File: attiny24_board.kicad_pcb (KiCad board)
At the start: 2 copper layers, 11 parts, among them J1 SPI, J2 OUT, J3 SCKLED, J4 CONN_01X02, U1 ATTINY24A-SSU, Y1 12000

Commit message: Make changes
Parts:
- moved C1 93.2 mm to (34.3, 32.0)
- moved J4 93.2 mm to (34.3, 20.6)
- moved C2 93.2 mm to (35.8, 26.9)
- moved C3 93.2 mm to (24.6, 27.7)
- moved C4 93.2 mm to (29.0, 27.7)
- moved J1 93.2 mm to (24.1, 45.0)
- moved J3 93.2 mm to (44.5, 20.6)
- moved Y1 93.2 mm to (24.1, 32.0)
- moved D1 93.2 mm to (45.5, 26.7)
- moved J2 93.2 mm to (46.2, 32.3)
- moved U1 93.2 mm to (33.8, 41.6)
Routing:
- net GND: track 62.7 -> 45.5 mm
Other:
- board text added: "+"
- board text added: "-"
- board text added: "LED"
- board text added: "rst"
- board text added: "sck"
- board text added: "si"
- board text added: "so"

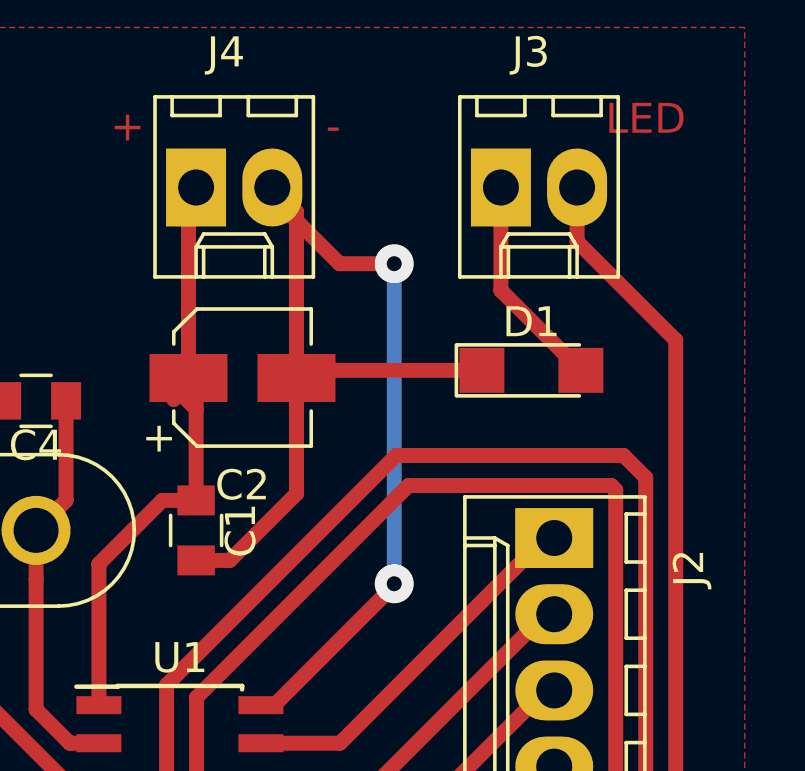
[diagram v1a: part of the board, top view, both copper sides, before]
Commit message: Add forgoteen resistor
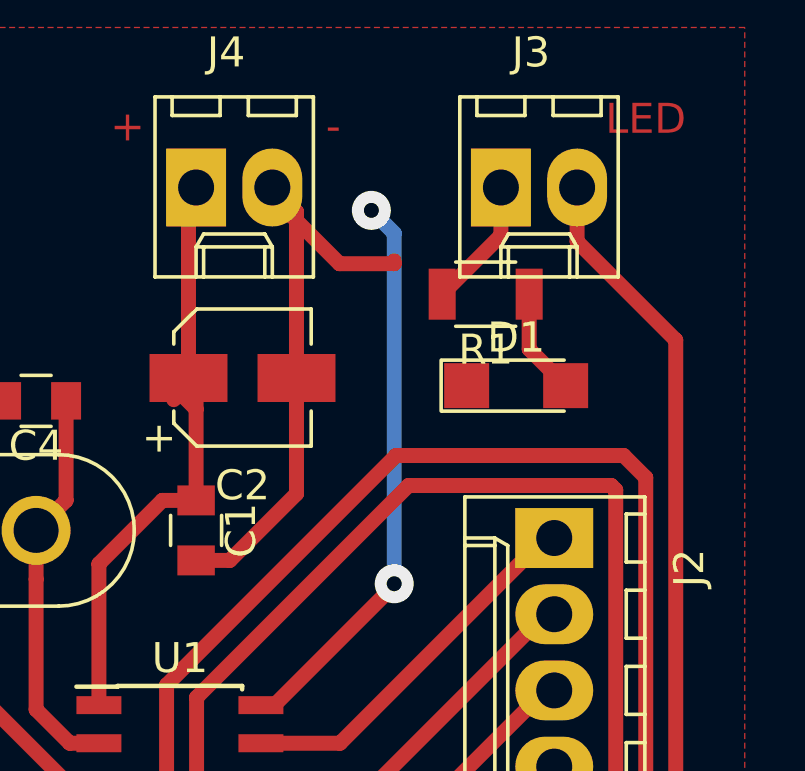
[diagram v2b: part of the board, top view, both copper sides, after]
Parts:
- added R1: 220, Resistors_SMD:R_1206, F.Cu at (43.9, 24.1)
- moved D1 0.72 mm to (45.0, 27.2)
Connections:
- J3 pad 1: Net-(D1-Pad2) -> Net-(J3-Pad1)
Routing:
- net Net-(J3-Pad1): track 0.00 -> 4.37 mm
- net GND: track 45.5 -> 41.8 mm
- net Net-(D1-Pad2): track 7.20 -> 3.55 mm
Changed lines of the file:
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@@
 (kicad_pcb (version 20170123) (host pcbnew "(2017-05-03 revision c70adcdf3)-master")
   (general
-    (links 25)
-    (no_connects 0)
-    (area 17.018 14.8165 52.578001 50.800001)
+    (links 26)
+    (no_connects 2)
+    (area 17.018 14.8165 52.684429 50.800001)
     (thickness 1.6)
     (drawings 7)
-    (tracks 95)
+    (tracks 98)
     (zones 0)
-    (modules 11)
-    (nets 16)
+    (modules 12)
+    (nets 17)
   )
   (page A4)
@@
   (net 14 /xtal1)
   (net 15 +3V3)
+  (net 16 "Net-(J3-Pad1)")
   (net_class Default "This is the default net class."
     (clearance 0.5)
@@
     (add_net "Net-(D1-Pad2)")
     (add_net "Net-(J2-Pad5)")
+    (add_net "Net-(J3-Pad1)")
+  )
+  (module Resistors_SMD:R_1206 (layer F.Cu)
+    (at 43.942 24.13 180)
+    (descr "Resistor SMD 1206, reflow soldering, Vishay (see dcrcw.pdf)")
+    (tags "resistor 1206")
+    (attr smd)
+    (fp_text reference R1 (at 0 -1.85 180) (layer F.SilkS)
+      (effects (font (size 1 1) (thickness 0.15)))
+    )
+    (fp_text value 220 (at -3.81 0 180) (layer F.Fab)
+      (effects (font (size 1 1) (thickness 0.15)))
+    )
+    (fp_line (start 2.15 1.1) (end -2.15 1.1) (layer F.CrtYd) (width 0.05))
+    (fp_line (start 2.15 1.1) (end 2.15 -1.11) (layer F.CrtYd) (width 0.05))
+    (fp_line (start -2.15 -1.11) (end -2.15 1.1) (layer F.CrtYd) (width 0.05))
+    (fp_line (start -2.15 -1.11) (end 2.15 -1.11) (layer F.CrtYd) (width 0.05))
+    (fp_line (start -1 -1.07) (end 1 -1.07) (layer F.SilkS) (width 0.12))
+    (fp_line (start 1 1.07) (end -1 1.07) (layer F.SilkS) (width 0.12))
+    (fp_line (start -1.6 -0.8) (end 1.6 -0.8) (layer F.Fab) (width 0.1))
+    (fp_line (start 1.6 -0.8) (end 1.6 0.8) (layer F.Fab) (width 0.1))
+    (fp_line (start 1.6 0.8) (end -1.6 0.8) (layer F.Fab) (width 0.1))
+    (fp_line (start -1.6 0.8) (end -1.6 -0.8) (layer F.Fab) (width 0.1))
+    (fp_text user %R (at 1.524 2.032 180) (layer F.Fab)
+      (effects (font (size 0.7 0.7) (thickness 0.105)))
+    )
+    (pad 2 smd rect (at 1.45 0 180) (size 0.9 1.7) (layers F.Cu F.Paste F.Mask)
+      (net 16 "Net-(J3-Pad1)"))
+    (pad 1 smd rect (at -1.45 0 180) (size 0.9 1.7) (layers F.Cu F.Paste F.Mask)
+      (net 2 "Net-(D1-Pad2)"))
+    (model ${KISYS3DMOD}/Resistors_SMD.3dshapes/R_1206.wrl
+      (at (xyz 0 0 0))
+      (scale (xyz 1 1 1))
+      (rotate (xyz 0 0 0))
+    )
   )
   (module Connectors_Molex:Molex_KK-6410-02_02x2.54mm_Straight (layer F.Cu)
@@
       (effects (font (size 1 1) (thickness 0.15)))
     )
-    (fp_text value SCKLED (at 1.27 4.5) (layer F.Fab)
+    (fp_text value SCKLED (at -0.762 -2.794) (layer F.Fab)
       (effects (font (size 1 1) (thickness 0.15)))
     )
@@
       (net 7 /sck))
     (pad 1 thru_hole rect (at 0 0) (size 2 2.6) (drill 1.2) (layers *.Cu *.Mask)
-      (net 2 "Net-(D1-Pad2)"))
+      (net 16 "Net-(J3-Pad1)"))
     (model ${KISYS3DMOD}/Connectors_Molex.3dshapes/Molex_KK-6410-02_02x2.54mm_Straight.wrl
       (at (xyz 0 0 0))
@@
   )
   (module LEDs:LED_1206 (layer F.Cu)
-    (at 45.466 26.67)
+    (at 44.958 27.178)
     (descr "LED 1206 smd package")
     (tags "LED led 1206 SMD smd SMT smt smdled SMDLED smtled SMTLED")
@@
       (effects (font (size 1 1) (thickness 0.15)))
     )
-    (fp_text value green (at 0 1.7) (layer F.Fab)
+    (fp_text value green (at 5.08 0) (layer F.Fab)
       (effects (font (size 1 1) (thickness 0.15)))
     )
@@
     (effects (font (size 1 1) (thickness 0.2)))
   )
+  (segment (start 40.894 33.782) (end 40.894 22.098) (width 0.5) (layer B.Cu) (net 1))
+  (segment (start 40.894 22.098) (end 40.132 21.336) (width 0.5) (layer B.Cu) (net 1))
+  (segment (start 40.894 23.017238) (end 40.894 23.114) (width 0.5) (layer F.Cu) (net 1))
   (segment (start 40.894 23.114) (end 39.07 23.114) (width 0.5) (layer F.Cu) (net 1))
   (segment (start 39.07 23.114) (end 36.83 20.874) (width 0.5) (layer F.Cu) (net 1))
   (segment (start 36.83 20.874) (end 36.83 20.574) (width 0.5) (layer F.Cu) (net 1))
-  (segment (start 40.894 33.782) (end 40.894 23.114) (width 0.5) (layer B.Cu) (net 1))
-  (via (at 40.894 23.114) (size 1.3) (drill 0.5) (layers F.Cu B.Cu) (net 1))
+  (via (at 40.132 21.336) (size 1.3) (drill 0.5) (layers F.Cu B.Cu) (net 1))
   (segment (start 36.450143 37.8285) (end 36.900143 37.8285) (width 0.5) (layer F.Cu) (net 1))
   (segment (start 36.900143 37.8285) (end 40.894 33.834643) (width 0.5) (layer F.Cu) (net 1))
@@
   (segment (start 37.636 26.924) (end 37.636 21.38) (width 0.5) (layer F.Cu) (net 1))
   (segment (start 37.636 21.38) (end 36.83 20.574) (width 0.5) (layer F.Cu) (net 1))
-  (segment (start 43.816 26.67) (end 37.89 26.67) (width 0.5) (layer F.Cu) (net 1))
   (segment (start 37.89 26.67) (end 37.636 26.924) (width 0.5) (layer F.Cu) (net 1))
   (segment (start 25.638 27.686) (end 27.956 27.686) (width 0.5) (layer F.Cu) (net 1))
-  (segment (start 44.45 20.574) (end 44.45 24.004) (width 0.5) (layer F.Cu) (net 2))
-  (segment (start 44.45 24.004) (end 47.116 26.67) (width 0.5) (layer F.Cu) (net 2))
+  (segment (start 45.392 24.13) (end 45.392 25.962) (width 0.5) (layer F.Cu) (net 2))
+  (segment (start 45.392 25.962) (end 46.608 27.178) (width 0.5) (layer F.Cu) (net 2))
   (segment (start 36.450143 39.0985) (end 39.0875 39.0985) (width 0.5) (layer F.Cu) (net 3))
   (segment (start 39.0875 39.0985) (end 45.928 32.258) (width 0.5) (layer F.Cu) (net 3))
@@
   (segment (start 33.165 31.004) (end 34.29 31.004) (width 0.5) (layer F.Cu) (net 15))
   (segment (start 33.544 27.648) (end 33.76 27.432) (width 0.5) (layer F.Cu) (net 15))
+  (segment (start 44.45 20.574) (end 44.45 22.172) (width 0.5) (layer F.Cu) (net 16))
+  (segment (start 44.45 22.172) (end 42.492 24.13) (width 0.5) (layer F.Cu) (net 16))
   (zone (net 1) (net_name GND) (layer F.Cu) (hatch edge 0.508)
     (connect_pads (clearance 0.508))
